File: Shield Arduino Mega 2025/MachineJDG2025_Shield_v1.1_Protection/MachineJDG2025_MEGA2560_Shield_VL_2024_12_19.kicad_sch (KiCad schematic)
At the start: 40 parts, among them J1 XT60PW-M, J2 Screw_Terminal_01x04, J3 Screw_Terminal_01x04, J4 Screw_Terminal_01x04, J5 Screw_Terminal_01x04, J6 SSW-103-01-F-D, J7 691214110002, Q1 MMBT3904, Q2 AOD4185, U1 MEGA_PRO_EMBED_CH340G___ATMEG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, U2 XL4016, U3 XL4016

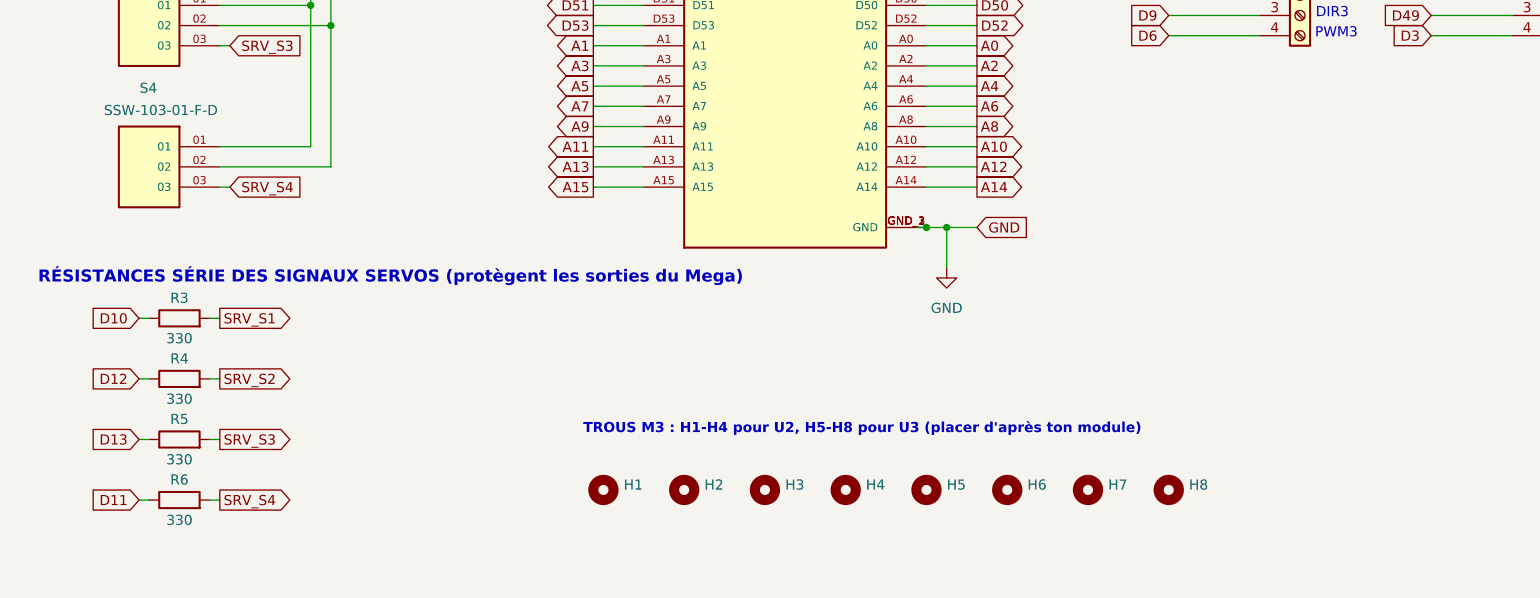
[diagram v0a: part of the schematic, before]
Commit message: Shield JDG2025 v1.1 : ajout des servos S5 (D44) et S6 (D45)
- Embases S5/S6 identiques à S1-S4 sur le rail 6 V protégé (bus GND/6V prolongés)
- R8/R9 330 ohms 0805 en série sur les signaux (SRV_S5, SRV_S6)
- Bloc des résistances servos et trous M3 déplacés pour faire de la place ;
  les UUID des symboles de la v1.1 sont conservés
- BOM JLCPCB (330R x6), liste des pièces à souder, PDF et LISEZMOI mis à jour

Co-Authored-By: Claude Opus 5.5 <noreply@anthropic.com>
Claude-Session: https://claude.ai/code/session_014Hmn23FgQ8XkTXPYbwms5W
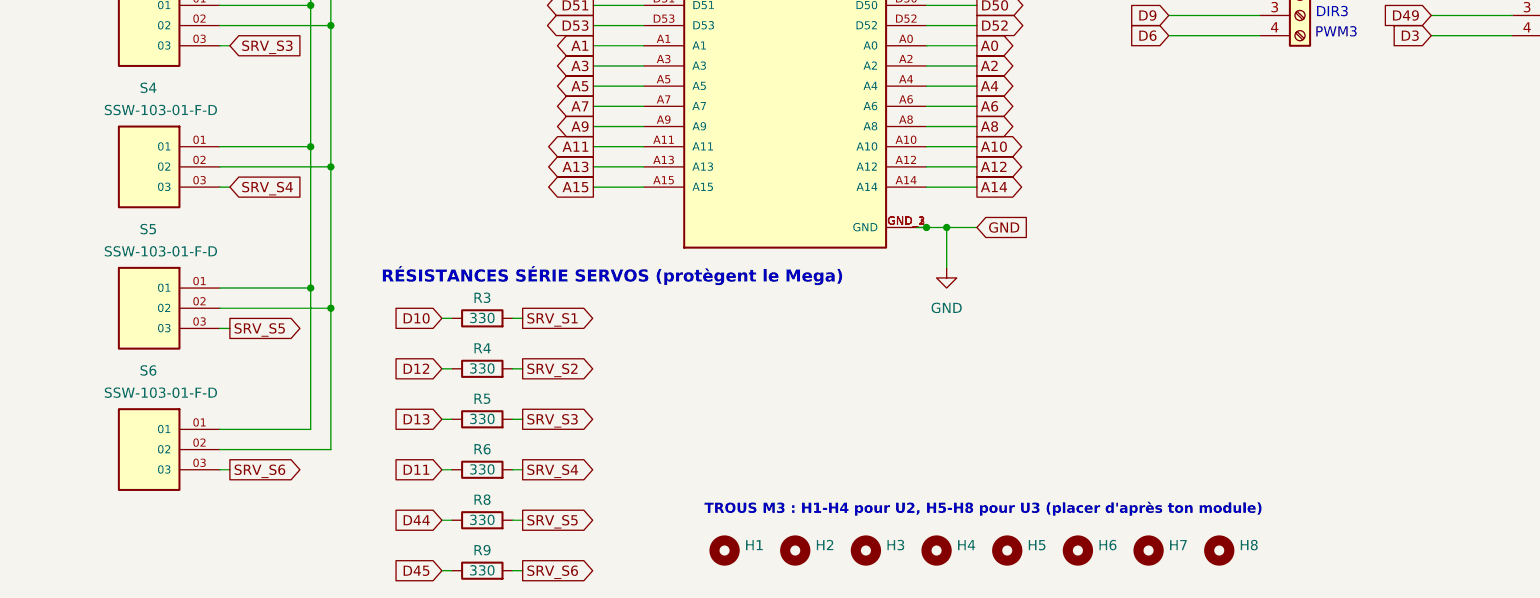
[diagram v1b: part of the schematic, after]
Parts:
- added R8, R9: 330, Resistor_SMD:R_0805_2012Metric, symbol Device:R
- added S5, S6: SSW-103-01-F-D, KiCad_Symbol_Custom:SAMTEC_SSW-103-01-F-D_3X1, symbol SSW-103-01-F-D:SSW-103-01-F-D_3X1
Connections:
- net 6V: now also S5.02, S6.02
- net D44: now also R8.1
- net D45: now also R9.1
- net GND: now also S5.01, S6.01
- new net SRV_S5: R8.2, S5.03
- new net SRV_S6: R9.2, S6.03
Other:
- note added: "RÉSISTANCES SÉRIE SERVOS (protègent le Mega)"
- note removed: "RÉSISTANCES SÉRIE DES SIGNAUX SERVOS (protègent les sorties du Mega)"
- moved on the sheet: H1, H2, H3, H4, H5, H6, H7, H8, R3, R4, R5, R6

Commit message: Shield JDG2025 v1.1 : modules XL4005 soudés à plat au lieu des XL4016 câblés
- U2/U3 : modules XL4005 5 A (carte 43 x 21 mm type DSN5000), nouvelle empreinte
  JDG_Protection:XL4005_Module_Flat avec la même origine et les mêmes pastilles
  (entraxe 40 x 17,5 mm) que l'ancienne empreinte LM2596, pastilles de 3 mm
- Empreinte XL4016_Module_Wired et trous M3 H1-H8 retirés
- F1 passe à 7,5 A (module 5 A) ; UUID des autres symboles conservés
- Liste des pièces à souder, LISEZMOI (montage sur pattes 1 mm, réglage) et PDF à jour

Co-Authored-By: Claude Opus 5.5 <noreply@anthropic.com>
Claude-Session: https://claude.ai/code/session_014Hmn23FgQ8XkTXPYbwms5W
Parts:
- removed H1, H2, H3, H4, H5, H6, H7, H8: MountingHole, MountingHole:MountingHole_3.2mm_M3, symbol Mechanical:MountingHole
- F1: value Mini-lame 10A -> Mini-lame 7.5A
- U2, U3: value XL4016 -> XL4005; footprint JDG_Protection:XL4016_Module_Wired -> JDG_Protection:XL4005_Module_Flat
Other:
- note added: "PROTECTION RAIL SERVOS 6 V (U2 -> F1 -> S1-S6)"
- note added: "Réglage au pot : U2 = 6,0 V U3 = 5,0 V"
- note added: "U2, U3 = modules XL4005 5 A (43 x 21 mm) soudés"
- note added: "à plat sur 4 pattes en fil de cuivre 1 mm"
- note removed: "PROTECTION RAIL SERVOS 6 V (U2 -> F1 -> S1-S4)"
- note removed: "TROUS M3 : H1-H4 pour U2, H5-H8 pour U3 (placer d'après ton module)"
- note removed: "U2 : 6,0 V / CC ~8 A U3 : 5,0 V / CC ~2,5 A"
- note removed: "U2, U3 = modules XL4016 sur entretoises M3,"
- note removed: "reliés par fils (empreinte JDG_Protection)"

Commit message: Shield JDG2025 v1.1 : U2/U3 acceptent un XL4005 ou un LM2596 (43 x 21 mm)
- Valeur de U2/U3 : "XL4005 / LM2596 (43x21)", description et note du schéma à jour
- Empreinte XL4005_Module_Flat : description et texte F.Fab mentionnent les deux modules
- LISEZMOI : tableau XL4005 vs LM2596, alignement du IN+ avant soudure, fil 0,8-1 mm
- Liste des pièces à souder à jour

Co-Authored-By: Claude Opus 5.5 <noreply@anthropic.com>
Claude-Session: https://claude.ai/code/session_014Hmn23FgQ8XkTXPYbwms5W
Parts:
- U2, U3: value XL4005 -> XL4005 / LM2596 (43x21)
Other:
- note added: "U2, U3 = XL4005 (5 A) ou LM2596 (3 A), 43 x 21 mm,"
- note added: "soudés à plat sur 4 pattes en fil de cuivre"
- note removed: "U2, U3 = modules XL4005 5 A (43 x 21 mm) soudés"
- note removed: "à plat sur 4 pattes en fil de cuivre 1 mm"
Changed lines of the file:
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@@
 			)
 		)
-		(property "Value" "XL4005"
+		(property "Value" "XL4005 / LM2596 (43x21)"
 			(at 162.56 26.67 0)
 			(show_name no)
@@
 			)
 		)
-		(property "Description" "Module buck XL4005 5 A (carte 43 x 21 mm type DSN5000), soudé à plat sur 4 pattes"
+		(property "Description" "Module buck 43 x 21 mm soudé à plat sur 4 pattes : XL4005 5 A (DSN5000) ou LM2596 3 A (DSN2596)"
 			(at 163.83 31.75 0)
 			(hide yes)
@@
 			)
 		)
-		(property "Value" "XL4005"
+		(property "Value" "XL4005 / LM2596 (43x21)"
 			(at 162.56 44.45 0)
 			(show_name no)
@@
 			)
 		)
-		(property "Description" "Module buck XL4005 5 A (carte 43 x 21 mm type DSN5000), soudé à plat sur 4 pattes"
+		(property "Description" "Module buck 43 x 21 mm soudé à plat sur 4 pattes : XL4005 5 A (DSN5000) ou LM2596 3 A (DSN2596)"
 			(at 163.83 49.53 0)
 			(hide yes)
@@
 		)
 	)
-	(text "U2, U3 = modules XL4005 5 A (43 x 21 mm) soudés"
+	(text "U2, U3 = XL4005 (5 A) ou LM2596 (3 A), 43 x 21 mm,"
 		(exclude_from_sim no)
 		(at 140.97 60.96 0)
@@
 		)
 	)
-	(text "à plat sur 4 pattes en fil de cuivre 1 mm"
+	(text "soudés à plat sur 4 pattes en fil de cuivre"
 		(exclude_from_sim no)
 		(at 140.97 63.5 0)

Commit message: Shield JDG2025 v1.1 : empreinte XL4005_DC-DC fournie pour U2/U3
- Empreinte KiCad-master/library/Module/XL4005/XL4005_DC-DC convertie au
  format KiCad 10 (pastilles et sérigraphie inchangées, courtyard ajoutée),
  remplace XL4005_Module_Flat dans JDG_Protection.pretty
- U2/U3 pointent sur JDG_Protection:XL4005_DC-DC ; note du schéma à jour
- LISEZMOI et liste des pièces : entraxe 39,5 x 17,15 mm, perçage 1,2 mm,
  2 vis M3 nylon + entretoises 3 mm par module

Co-Authored-By: Claude Opus 5.5 <noreply@anthropic.com>
Claude-Session: https://claude.ai/code/session_014Hmn23FgQ8XkTXPYbwms5W
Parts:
- U2, U3: footprint JDG_Protection:XL4005_Module_Flat -> JDG_Protection:XL4005_DC-DC
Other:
- note added: "soudés à plat : 4 pattes en fil + 2 vis M3 nylon"
- note removed: "soudés à plat sur 4 pattes en fil de cuivre"
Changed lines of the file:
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@@
 			)
 		)
-		(property "Footprint" "JDG_Protection:XL4005_Module_Flat"
+		(property "Footprint" "JDG_Protection:XL4005_DC-DC"
 			(at 163.83 31.75 0)
 			(hide yes)
@@
 			)
 		)
-		(property "Description" "Module buck 43 x 21 mm soudé à plat sur 4 pattes : XL4005 5 A (DSN5000) ou LM2596 3 A (DSN2596)"
+		(property "Description" "Module buck 43 x 21 mm soudé à plat sur 4 pattes (+2 vis M3) : XL4005 5 A ou LM2596 3 A, même carte"
 			(at 163.83 31.75 0)
 			(hide yes)
@@
 			)
 		)
-		(property "Footprint" "JDG_Protection:XL4005_Module_Flat"
+		(property "Footprint" "JDG_Protection:XL4005_DC-DC"
 			(at 163.83 49.53 0)
 			(hide yes)
@@
 			)
 		)
-		(property "Description" "Module buck 43 x 21 mm soudé à plat sur 4 pattes : XL4005 5 A (DSN5000) ou LM2596 3 A (DSN2596)"
+		(property "Description" "Module buck 43 x 21 mm soudé à plat sur 4 pattes (+2 vis M3) : XL4005 5 A ou LM2596 3 A, même carte"
 			(at 163.83 49.53 0)
 			(hide yes)
@@
 		)
 	)
-	(text "soudés à plat sur 4 pattes en fil de cuivre"
+	(text "soudés à plat : 4 pattes en fil + 2 vis M3 nylon"
 		(exclude_from_sim no)
 		(at 140.97 63.5 0)

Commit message: Shield JDG2025 v1.1 : protections simplifiées (TVS + condensateurs)
- Retire l'anti-inversion Q2/R7/D1 : J1 (XT60) va directement sur le 12V ;
  une inversion fait conduire D2 et sauter le fusible 15 A du fil batterie
- Retire les porte-fusibles F1/F2 : les sorties des modules retrouvent
  leurs étiquettes 6V et 5V_AUX
- Garde les TVS D2/D3/D4 et les condensateurs C1/C2/C3 ; UUID conservés
- BOM JLCPCB (10 lignes, 15 pièces), liste des pièces, classes de nets,
  LISEZMOI et PDF à jour

Co-Authored-By: Claude Opus 5.5 <noreply@anthropic.com>
Claude-Session: https://claude.ai/code/session_014Hmn23FgQ8XkTXPYbwms5W
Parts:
- removed D1: BZT52C15, Diode_SMD:D_SOD-123, symbol Device:D_Zener
- removed F1: Mini-lame 7.5A, Fuse:Fuseholder_Blade_Mini_Keystone_3568, symbol Device:Fuse
- removed F2: Mini-lame 3A, Fuse:Fuseholder_Blade_Mini_Keystone_3568, symbol Device:Fuse
- removed Q2: AOD4185, Package_TO_SOT_SMD:TO-252-2, symbol Transistor_FET:Q_PMOS_GDS
- removed R7: 47k, Resistor_SMD:R_0805_2012Metric, symbol Device:R
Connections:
- net 5V_AUX_MOD is gone; now on net 5V_AUX: U3.3 (Vout+)
- net 6V_MOD is gone; now on net 6V: U2.3 (Vout+)
- net BAT+ is gone; now on net 12V: J1.2 (Pin_2)
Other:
- note added: "Inversion : D2 conduit et fait sauter le fusible 15 A"
- note added: "PROTECTION RAIL SERVOS 6 V (TVS + condensateur)"
- note added: "PROTECTION SORTIE 5V_AUX (TVS + condensateur)"
- note removed: "PROTECTION RAIL SERVOS 6 V (U2 -> F1 -> S1-S6)"
- note removed: "PROTECTION SORTIE 5V_AUX (U3 -> F2 -> J7)"
